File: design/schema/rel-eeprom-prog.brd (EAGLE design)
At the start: 92.4 x 59.7 mm, 4 parts, among them IC2 74HC595N, IC3 74HC595N

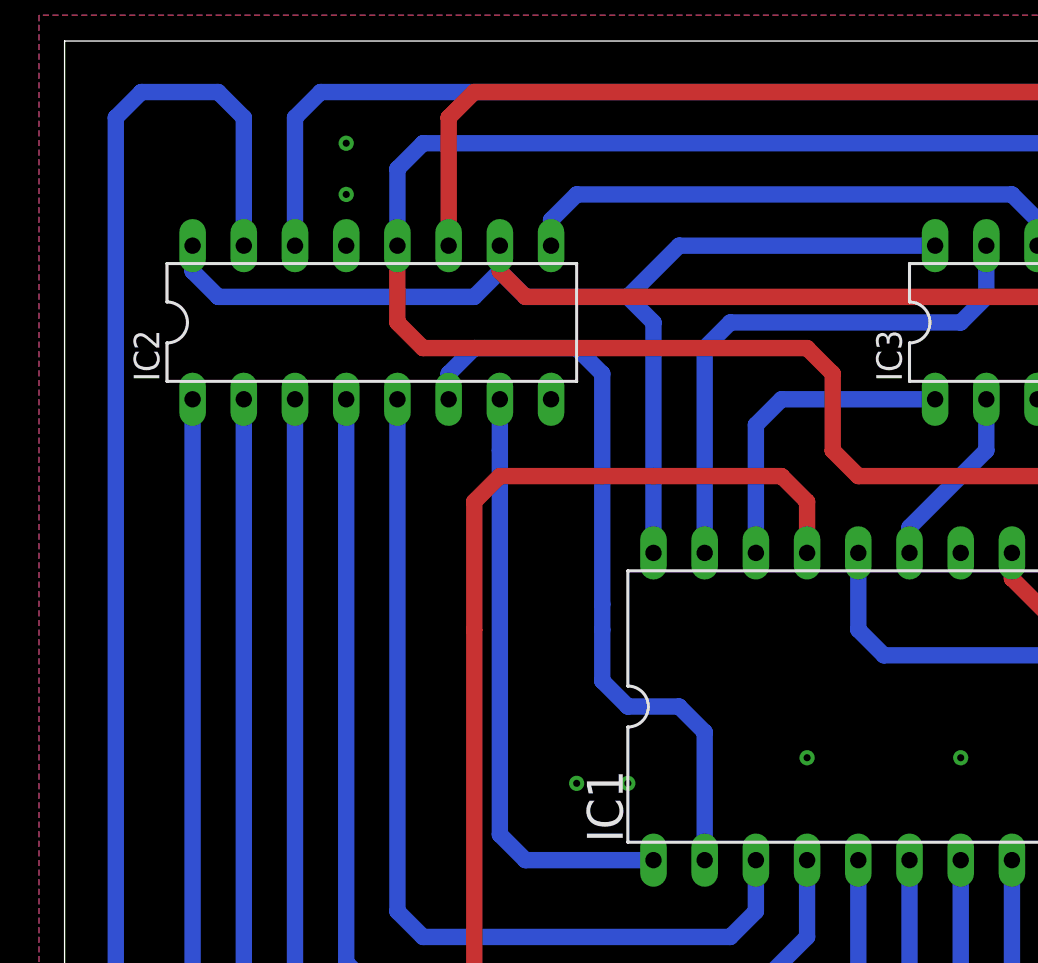
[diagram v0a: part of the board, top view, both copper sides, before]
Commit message: Updated IC chips names
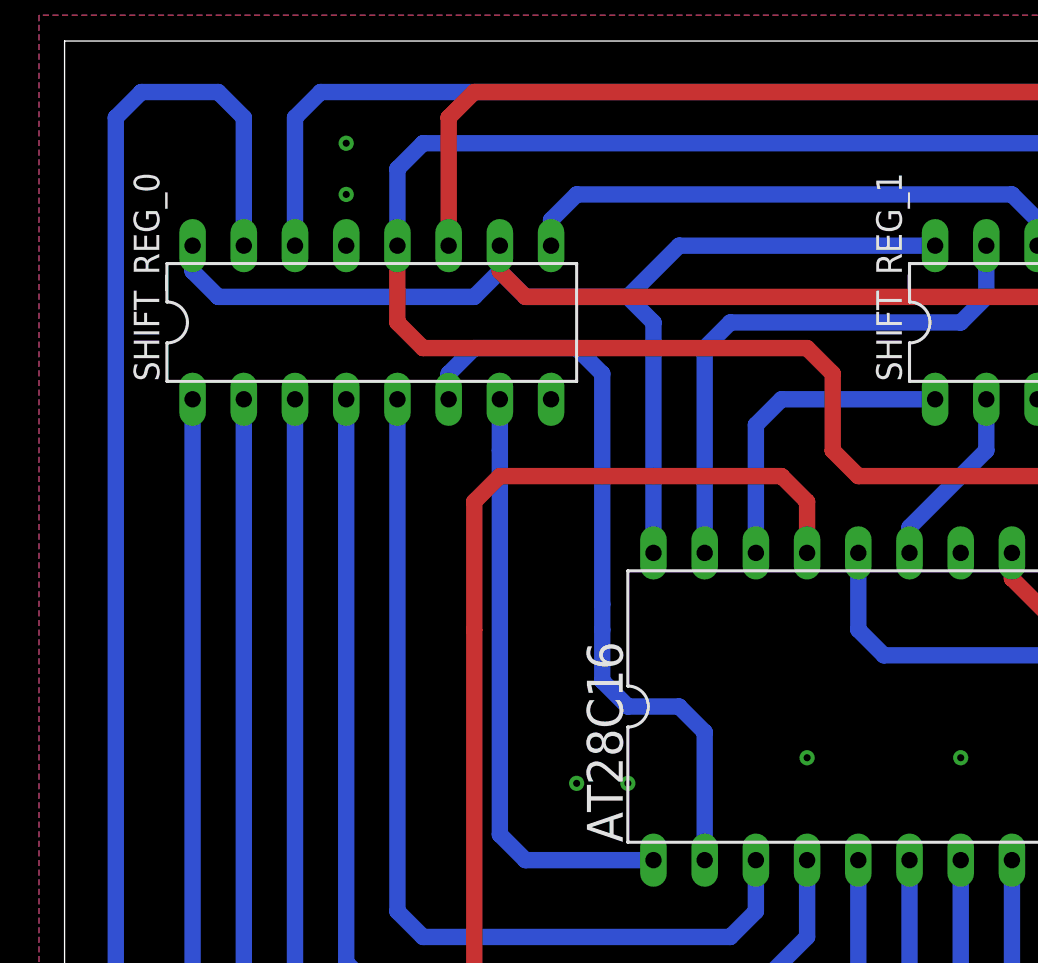
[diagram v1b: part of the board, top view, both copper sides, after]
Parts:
- renumbered IC1 to AT28C16, IC2 to SHIFT_REG_0, IC3 to SHIFT_REG_1
